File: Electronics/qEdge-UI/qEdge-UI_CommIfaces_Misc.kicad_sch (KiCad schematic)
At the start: 33 parts, among them IC501 74HC4066PW, IC502 74HC4066PW, IC503 74HC4066PW, IC504 74HC4066PW, IC505 74HC4066PW, IC506 74HC4066PW, IC507 74HC4066PW, J501 SMA_EdgeMount, Q501 BSS138BKW, Q502 BSS138BKW, Q503 BSS138BKW, U501 RFM95W-868S2, U503 SP3485CN

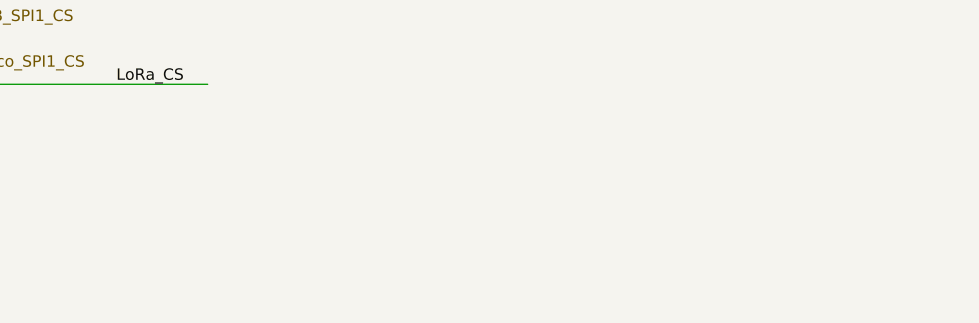
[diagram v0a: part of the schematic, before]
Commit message: added READMEs for Mechanic and Electronic added License in the Electronic schematics restructured Mechanics for better readability and reproducibility
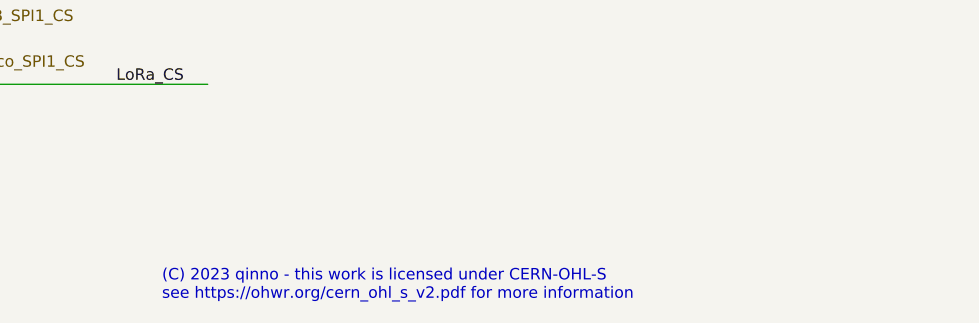
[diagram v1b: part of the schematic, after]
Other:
- note added: "(C) 2023 qinno - this work is licensed under CERN-OHL-S see https://ohwr.org/cern_ohl_s_v2.pdf for more information"
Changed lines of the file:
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@@
     (effects (font (size 0.762 0.762)) (justify left bottom))
+  )
+  (text "(C) 2023 qinno - this work is licensed under CERN-OHL-S\nsee https://ohwr.org/cern_ohl_s_v2.pdf for more information"
+    (at 238.76 283.21 0)
+    (effects (font (size 1.27 1.27)) (justify left bottom))
   )
   (text "SPI-control soldering jumper" (at 35.56 219.71 0)
